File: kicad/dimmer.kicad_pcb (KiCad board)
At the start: 2 copper layers, 12 parts, among them IC1 ATTINY85-P, P1 CONN_01X02, P2 CONN_01X02, Q1 Q_NMOS_GDS, SW1 TACTILE_SW, SW2 TACTILE_SW, SW3 TACTILE_SW, SW4 TACTILE_SW, U1 MC78L05ACH

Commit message: pcb progress
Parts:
- removed SW1, SW3: TACTILE_SW, Buttons_Switches_ThroughHole:SW_TH_Tactile_Omron_B3F-10xx
- moved U1 12.7 mm to (201.9, 127.6)
- moved SW4 8.28 mm to (204.5, 123.8), turned to 180 degrees
- moved C1 8.15 mm to (201.2, 132.1), turned to 180 degrees
- moved C2 6.35 mm to (197.5, 131.4)
- moved SW2 4.26 mm to (198.1, 134.6)
- moved R1 3.81 mm to (197.5, 127.0), turned to 90 degrees
- moved Q1 3.24 mm to (188.6, 128.9), turned to 0 degrees
- moved IC1 1.91 mm to (193.7, 129.5), turned to 270 degrees
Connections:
- IC1 pad 5: Net-(IC1-Pad5) -> (no net)
- IC1 pad 7: Net-(IC1-Pad7) -> (no net)
- P1 pad 1: GND -> +12V
- P1 pad 2: +12V -> GND
- SW4 pad 1: Net-(IC1-Pad2) -> (no net)
- SW4 pad 2: (no net) -> Net-(IC1-Pad2)
- SW4 pad 3: GND -> (no net)
- SW4 pad 4: (no net) -> GND
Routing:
- net +12V: track 0.00 -> 52.1 mm
- net GND: track 0.00 -> 41.5 mm
- net +5V: track 0.00 -> 37.3 mm
- net /out: track 0.00 -> 8.84 mm
- net Net-(IC1-Pad3): track 0.00 -> 7.98 mm
- net Net-(IC1-Pad2): track 0.00 -> 7.48 mm
- net Net-(IC1-Pad6): track 0.00 -> 6.77 mm
- net Net-(IC1-Pad1): track 0.00 -> 3.39 mm
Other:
- net class Load added: clearance 0.2, trace_width 1.5, via_dia 1.5, via_drill 0.8
- net class Power added: clearance 0.2, trace_width 0.5, via_dia 0.8, via_drill 0.6

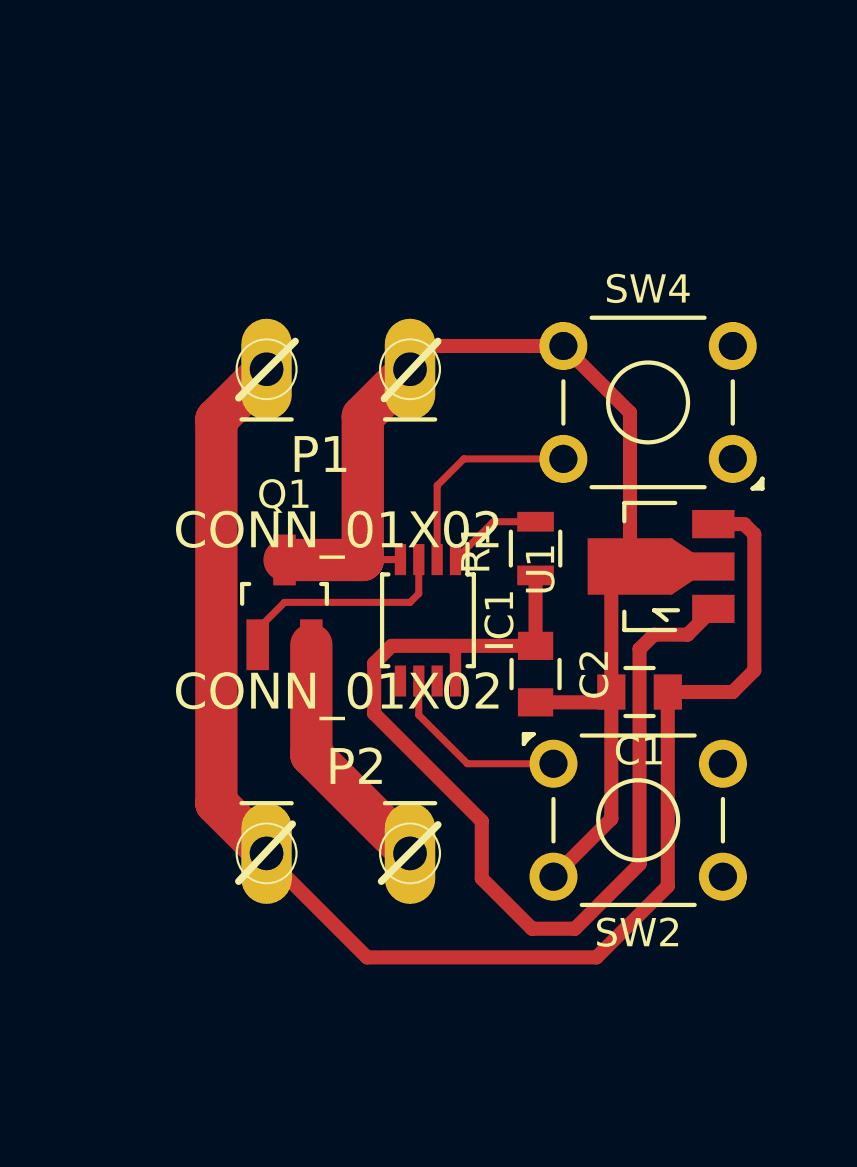
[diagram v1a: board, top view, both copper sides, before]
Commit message: pcb: changing sides
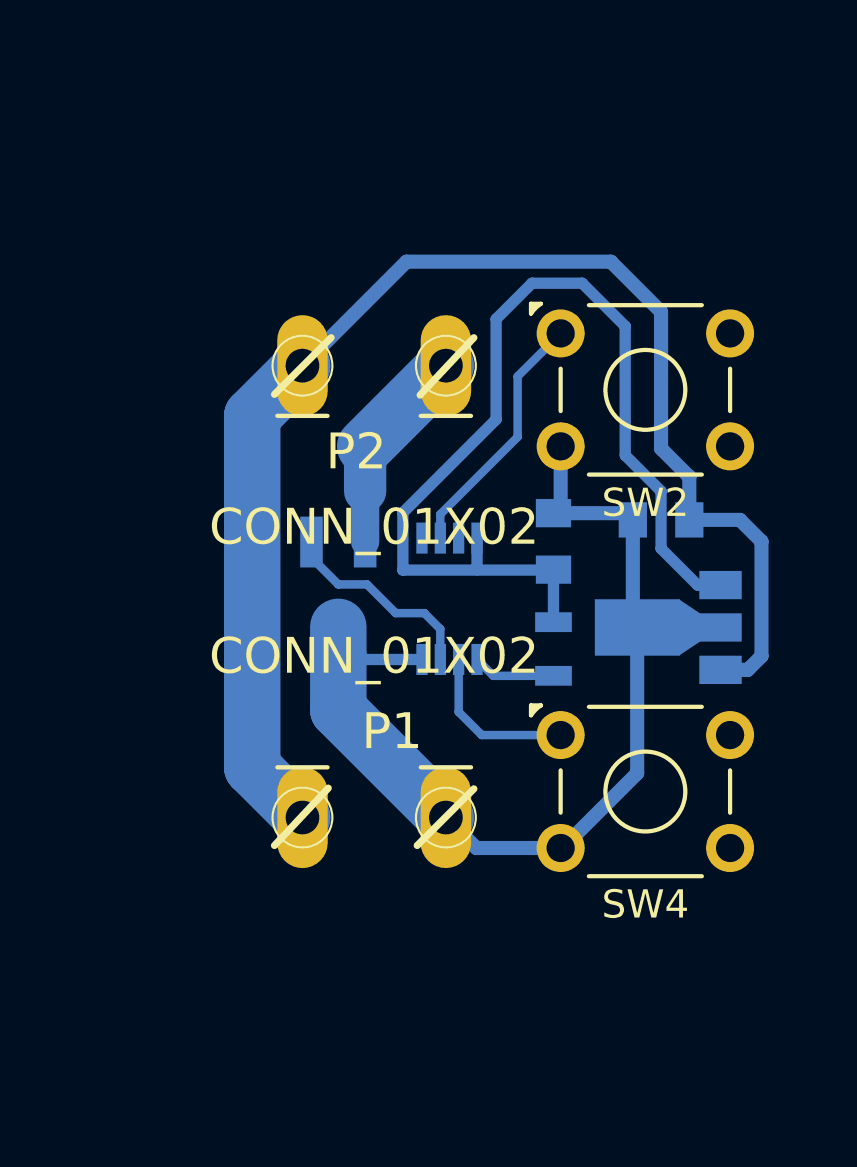
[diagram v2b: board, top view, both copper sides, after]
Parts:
- C1, C2, IC1, Q1, R1, U1: moved to B.Cu
- moved P2 18.6 mm to (191.8, 119.9), turned to 0 degrees
- moved P1 17.2 mm to (191.8, 137.2), turned to 180 degrees
- moved SW2 15.2 mm to (198.4, 119.4)
- moved SW4 11.5 mm to (198.4, 133.6), turned to 0 degrees
- moved C1 6.14 mm to (201.9, 126.0)
- moved C2 4.74 mm to (198.1, 126.7), turned to 90 degrees
- moved R1 3.61 mm to (198.1, 130.6), turned to 270 degrees
- moved U1 2.17 mm to (202.2, 129.8), turned to 270 degrees
- moved Q1 2.01 mm to (190.5, 128.3)
- moved IC1 1.08 mm to (194.4, 128.8), turned to 90 degrees
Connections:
- P1 pad 1: +12V -> GND
- P1 pad 2: GND -> +12V
- P2 pad 1: /out -> +12V
- P2 pad 2: +12V -> /out
- SW4 pad 1: (no net) -> Net-(IC1-Pad2)
- SW4 pad 2: Net-(IC1-Pad2) -> (no net)
- SW4 pad 3: (no net) -> GND
- SW4 pad 4: GND -> (no net)
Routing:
- net GND: track 41.5 -> 35.1 mm
- net +12V: track 52.1 -> 48.9 mm
- net Net-(IC1-Pad6): track 6.77 -> 9.09 mm
- net +5V: track 37.3 -> 35.3 mm
- net Net-(IC1-Pad2): track 7.48 -> 5.81 mm
- net /out: track 8.84 -> 7.43 mm
- net Net-(IC1-Pad3): track 7.98 -> 7.24 mm
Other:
- net class 5V added: clearance 0.2, trace_width 0.4, via_dia 0.6, via_drill 0.4
- net class Default: trace_width 0.25 -> 0.3

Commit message: pcb: proper t85 footprint
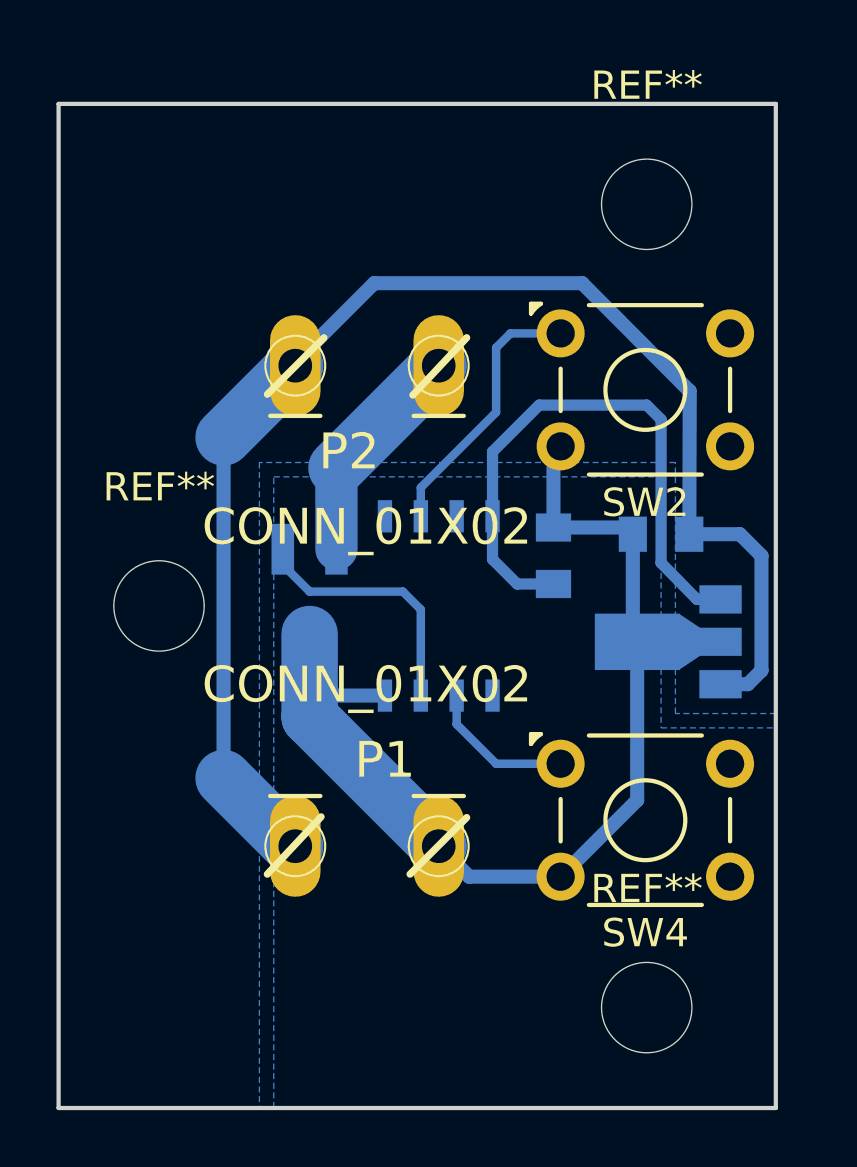
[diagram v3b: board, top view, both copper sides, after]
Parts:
- removed R1: 10k, Resistors_SMD:R_0805
- added REF**: MountingHole_3.2mm_M3, Mounting_Holes:MountingHole_3.2mm_M3, F.Cu at (201.4, 143.3)
- added REF**: MountingHole_3.2mm_M3, Mounting_Holes:MountingHole_3.2mm_M3, F.Cu at (201.4, 114.8)
- added REF**: MountingHole_3.2mm_M3, Mounting_Holes:MountingHole_3.2mm_M3, F.Cu at (184.2, 129.0)
- IC1: value ATTINY85-P -> ATTINY85-S; footprint Housings_SSOP:TSSOP-8_3x3mm_Pitch0.65mm -> SMD_Packages:SOIC-8-N
- moved P1 1.05 mm to (191.5, 138.2)
- moved Q1 1.05 mm to (189.5, 128.5)
- moved SW4 1.02 mm to (198.4, 134.6)
- moved C1 0.51 mm to (201.9, 126.5)
- moved C2 0.51 mm to (198.1, 127.3)
- moved U1 0.51 mm to (202.2, 130.3)
- moved IC1 0.46 mm to (194.1, 129.0), turned to 180 degrees
- moved P2 0.25 mm to (191.5, 119.9)
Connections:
- IC1 pad 1: Net-(IC1-Pad1) -> (no net)
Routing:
- net +5V: track 35.3 -> 20.9 mm
- net GND: track 35.1 -> 39.8 mm
- net Net-(IC1-Pad1): track 2.95 -> 0.00 mm
- net Net-(IC1-Pad3): track 7.24 -> 9.14 mm
- net +12V: track 48.9 -> 49.7 mm
- net /out: track 7.43 -> 8.00 mm
- net Net-(IC1-Pad2): track 5.81 -> 5.28 mm
- added copper zone on B.Cu, net +12V
- added copper zone on B.Cu, net GND
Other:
- board outline added: 25.4 x 35.6 mm
